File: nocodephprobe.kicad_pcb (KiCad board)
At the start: 2 copper layers, 76 x 80.9 mm, 34 parts, among them J1 RF1-01 BNC, J2 10K, Q1 2N7002, U1 LMV358a, U2 ICL7106CPL, U3 MCP1501T-10E/CHY, U4 VI-302-DP-RC-S, U5 L7805

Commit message: Remove fmask all the way around guard trace
Based on prototype pcbs from jlcpcb, I don't think solder bridges will
be an issue.
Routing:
- net BP: track 127.5 -> 125.7 mm, vias 3 -> 2
- net Net-(U2-INT): track 35.8 -> 35.0 mm
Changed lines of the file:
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@@
   (gr_line (start 122.297226 85.580302) (end 122.29625 85.580045)
     (stroke (width 0.132291) (type solid)) (layer "B.SilkS"))
+  (gr_line (start 156.9466 64.4906) (end 157.48 64.008)
+    (stroke (width 0.153) (type default)) (layer "F.Mask"))
   (gr_line (start 154.6098 64.389) (end 151.384 64.4144)
     (stroke (width 0.25) (type default)) (layer "F.Mask"))
+  (gr_line (start 159.766 63.754) (end 159.766 62.992)
+    (stroke (width 0.153) (type default)) (layer "F.Mask"))
+  (gr_line (start 149.606 67.818) (end 149.86 67.564)
+    (stroke (width 0.153) (type default)) (layer "F.Mask"))
+  (gr_line (start 159.766 62.992) (end 159.004 62.23)
+    (stroke (width 0.153) (type default)) (layer "F.Mask"))
+  (gr_line (start 157.48 64.008) (end 159.512 64.008)
+    (stroke (width 0.153) (type default)) (layer "F.Mask"))
+  (gr_line (start 149.86 67.564) (end 150.368 67.5132)
+    (stroke (width 0.153) (type default)) (layer "F.Mask"))
+  (gr_line (start 150.1648 65.532) (end 148.336 65.532)
+    (stroke (width 0.153) (type default)) (layer "F.Mask"))
+  (gr_line (start 148.082 67.818) (end 149.606 67.818)
+    (stroke (width 0.153) (type default)) (layer "F.Mask"))
   (gr_line (start 150.368 67.5132) (end 152.1714 65.786)
     (stroke (width 0.25) (type default)) (layer "F.Mask"))
@@
   (gr_line (start 158.2674 62.103) (end 157 62.103)
     (stroke (width 0.25) (type default)) (layer "F.Mask"))
+  (gr_line (start 148.336 65.532) (end 147.574 66.294)
+    (stroke (width 0.153) (type default)) (layer "F.Mask"))
+  (gr_line (start 159.512 64.008) (end 159.766 63.754)
+    (stroke (width 0.153) (type default)) (layer "F.Mask"))
   (gr_line (start 151.384 64.4144) (end 150.1648 65.532)
     (stroke (width 0.25) (type default)) (layer "F.Mask"))
@@
   (gr_line (start 155.7274 65.8114) (end 156.9466 64.4906)
     (stroke (width 0.25) (type default)) (layer "F.Mask"))
+  (gr_line (start 147.574 67.31) (end 148.082 67.818)
+    (stroke (width 0.153) (type default)) (layer "F.Mask"))
+  (gr_line (start 147.574 66.294) (end 147.574 67.31)
+    (stroke (width 0.153) (type default)) (layer "F.Mask"))
   (gr_line (start 110.7891 63.5254) (end 110.7891 69.249537)
     (stroke (width 0.127) (type solid)) (layer "Edge.Cuts"))
@@
   (segment (start 153.67 69.596) (end 154.813 68.453) (width 0.25) (layer "B.Cu") (net 10))
   (segment (start 154.813 68.453) (end 165.989 68.453) (width 0.25) (layer "B.Cu") (net 10))
-  (segment (start 158.486695 80.264) (end 159.647695 79.103) (width 0.25) (layer "F.Cu") (net 11))
-  (segment (start 157.009 79.802305) (end 157.470695 80.264) (width 0.25) (layer "F.Cu") (net 11))
-  (segment (start 163.957 77.530009) (end 164.652009 76.835) (width 0.25) (layer "F.Cu") (net 11))
-  (segment (start 166.497 84.583396) (end 173.062604 91.149) (width 0.25) (layer "F.Cu") (net 11))
-  (segment (start 157.470695 80.264) (end 158.486695 80.264) (width 0.25) (layer "F.Cu") (net 11))
-  (segment (start 165.608 76.835) (end 166.497 77.724) (width 0.25) (layer "F.Cu") (net 11))
-  (segment (start 173.062604 91.149) (end 177.329 91.149) (width 0.25) (layer "F.Cu") (net 11))
-  (segment (start 163.025991 79.103) (end 163.957 78.171991) (width 0.25) (layer "F.Cu") (net 11))
-  (segment (start 157.48 77.978) (end 157.009 78.449) (width 0.25) (layer "F.Cu") (net 11))
-  (segment (start 157.009 78.449) (end 157.009 79.802305) (width 0.25) (layer "F.Cu") (net 11))
-  (segment (start 177.329 91.149) (end 178.435 90.043) (width 0.25) (layer "F.Cu") (net 11))
-  (segment (start 163.957 78.171991) (end 163.957 77.530009) (width 0.25) (layer "F.Cu") (net 11))
-  (segment (start 164.652009 76.835) (end 165.608 76.835) (width 0.25) (layer "F.Cu") (net 11))
-  (segment (start 166.497 77.724) (end 166.497 84.583396) (width 0.25) (layer "F.Cu") (net 11))
-  (segment (start 159.647695 79.103) (end 163.025991 79.103) (width 0.25) (layer "F.Cu") (net 11))
+  (segment (start 163.685 77.7674) (end 163.685 78.443991) (width 0.25) (layer "F.Cu") (net 11))
+  (segment (start 164.5994 76.853) (end 163.685 77.7674) (width 0.25) (layer "F.Cu") (net 11))
+  (segment (start 178.435 87.493695) (end 173.020305 82.079) (width 0.25) (layer "F.Cu") (net 11))
+  (segment (start 157.433695 80.227) (end 156.680001 79.473306) (width 0.25) (layer "F.Cu") (net 11))
+  (segment (start 166.8664 82.132) (end 166.225 81.4906) (width 0.25) (layer "F.Cu") (net 11))
+  (segment (start 159.114905 79.1464) (end 158.034305 80.227) (width 0.25) (layer "F.Cu") (net 11))
+  (segment (start 156.680001 78.777999) (end 157.48 77.978) (width 0.25) (layer "F.Cu") (net 11))
+  (segment (start 163.685 78.443991) (end 162.982591 79.1464) (width 0.25) (layer "F.Cu") (net 11))
+  (segment (start 156.680001 79.473306) (end 156.680001 78.777999) (width 0.25) (layer "F.Cu") (net 11))
+  (segment (start 167.6284 82.079) (end 167.5754 82.132) (width 0.25) (layer "F.Cu") (net 11))
+  (segment (start 173.020305 82.079) (end 167.6284 82.079) (width 0.25) (layer "F.Cu") (net 11))
+  (segment (start 162.982591 79.1464) (end 159.114905 79.1464) (width 0.25) (layer "F.Cu") (net 11))
+  (segment (start 167.5754 82.132) (end 166.8664 82.132) (width 0.25) (layer "F.Cu") (net 11))
+  (segment (start 178.435 90.043) (end 178.435 87.493695) (width 0.25) (layer "F.Cu") (net 11))
+  (segment (start 166.225 81.4906) (end 166.225 77.512009) (width 0.25) (layer "F.Cu") (net 11))
+  (segment (start 158.034305 80.227) (end 157.433695 80.227) (width 0.25) (layer "F.Cu") (net 11))
+  (segment (start 166.225 77.512009) (end 165.565991 76.853) (width 0.25) (layer "F.Cu") (net 11))
+  (segment (start 165.565991 76.853) (end 164.5994 76.853) (width 0.25) (layer "F.Cu") (net 11))
   (segment (start 178.689 117.586) (end 177.487 116.384) (width 0.25) (layer "F.Cu") (net 12))
   (segment (start 162.477 109.077) (end 161.9 108.5) (width 0.25) (layer "F.Cu") (net 12))
@@
   (segment (start 165.281 109.077) (end 162.477 109.077) (width 0.25) (layer "F.Cu") (net 12))
   (segment (start 143.315 101.435) (end 142.367 102.383) (width 0.25) (layer "F.Cu") (net 13))
+  (segment (start 172.72 100.858) (end 173.845 99.733) (width 0.25) (layer "F.Cu") (net 13))
   (segment (start 154.94 100.858) (end 153.865 101.933) (width 0.25) (layer "F.Cu") (net 13))
+  (segment (start 173.845 99.733) (end 173.845 83.929) (width 0.25) (layer "F.Cu") (net 13))
   (segment (start 145.855 100.41272) (end 145.22528 99.783) (width 0.25) (layer "F.Cu") (net 13))
-  (segment (start 172.72 82.804) (end 172.72 88.519) (width 0.25) (layer "F.Cu") (net 13))
   (segment (start 130.863297 71.681297) (end 142.504659 71.681297) (width 0.25) (layer "F.Cu") (net 13))
   (segment (start 172.72 100.858) (end 171.645 101.933) (width 0.25) (layer "F.Cu") (net 13))
@@
   (segment (start 129.54 70.358) (end 130.863297 71.681297) (width 0.25) (layer "F.Cu") (net 13))
   (segment (start 136.145 102.383) (end 134.62 100.858) (width 0.25) (layer "F.Cu") (net 13))
+  (segment (start 173.845 83.929) (end 172.72 82.804) (width 0.25) (layer "F.Cu") (net 13))
   (segment (start 127 70.358) (end 129.54 70.358) (width 0.25) (layer "F.Cu") (net 13))
   (segment (start 124.46 70.358) (end 127 70.358) (width 0.25) (layer "F.Cu") (net 13))
@@
   (segment (start 144.282 99.783) (end 143.315 100.75) (width 0.25) (layer "F.Cu") (net 13))
   (segment (start 171.645 101.933) (end 156.015 101.933) (width 0.25) (layer "F.Cu") (net 13))
-  (segment (start 172.72 88.519) (end 174.625 90.424) (width 0.25) (layer "F.Cu") (net 13))
   (segment (start 145.22528 99.783) (end 144.282 99.783) (width 0.25) (layer "F.Cu") (net 13))
   (via (at 172.72 82.804) (size 0.8) (drill 0.4) (layers "F.Cu" "B.Cu") (net 13))
   (via (at 142.504659 71.681297) (size 0.8) (drill 0.4) (layers "F.Cu" "B.Cu") (net 13))
-  (via (at 174.625 90.424) (size 0.8) (drill 0.4) (layers "F.Cu" "B.Cu") (net 13))
-  (segment (start 162.433 71.755) (end 163.83 71.755) (width 0.25) (layer "B.Cu") (net 13))
-  (segment (start 174.625 90.424) (end 174.625 94.644197) (width 0.25) (layer "B.Cu") (net 13))
-  (segment (start 163.83 71.755) (end 168.783 76.708) (width 0.25) (layer "B.Cu") (net 13))
-  (segment (start 168.783 76.708) (end 171.45 76.708) (width 0.25) (layer "B.Cu") (net 13))
-  (segment (start 161.163 69.977) (end 161.163 70.485) (width 0.25) (layer "B.Cu") (net 13))
-  (segment (start 174.625 94.644197) (end 172.72 96.549197) (width 0.25) (layer "B.Cu") (net 13))
-  (segment (start 161.163 70.485) (end 162.433 71.755) (width 0.25) (layer "B.Cu") (net 13))
-  (segment (start 156.015 69.283) (end 160.469 69.283) (width 0.25) (layer "B.Cu") (net 13))
+  (segment (start 172.72 77.978) (end 166.5932 71.8512) (width 0.25) (layer "B.Cu") (net 13))
+  (segment (start 156.4332 71.8512) (end 154.94 70.358) (width 0.25) (layer "B.Cu") (net 13))
+  (segment (start 166.5932 71.8512) (end 156.4332 71.8512) (width 0.25) (layer "B.Cu") (net 13))
   (segment (start 153.616703 71.681297) (end 154.94 70.358) (width 0.25) (layer "B.Cu") (net 13))
-  (segment (start 154.94 70.358) (end 156.015 69.283) (width 0.25) (layer "B.Cu") (net 13))
-  (segment (start 160.469 69.283) (end 161.163 69.977) (width 0.25) (layer "B.Cu") (net 13))
-  (segment (start 171.45 76.708) (end 172.72 77.978) (width 0.25) (layer "B.Cu") (net 13))
   (segment (start 142.504659 71.681297) (end 153.616703 71.681297) (width 0.25) (layer "B.Cu") (net 13))
-  (segment (start 172.72 96.549197) (end 172.72 100.858) (width 0.25) (layer "B.Cu") (net 13))
   (segment (start 172.72 82.804) (end 172.72 77.978) (width 0.25) (layer "B.Cu") (net 13))
   (segment (start 158.2166 58.2516) (end 158.2166 60.6022) (width 0.25) (layer "F.Cu") (net 14))

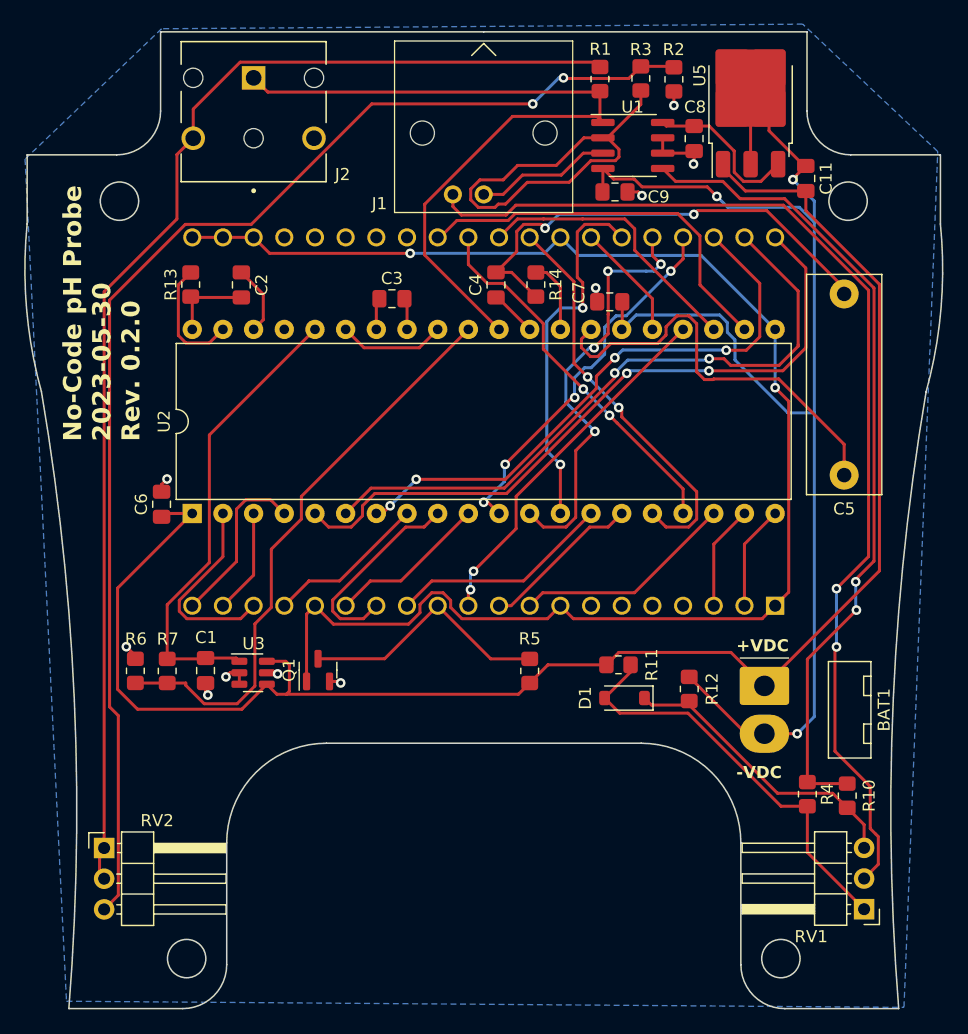
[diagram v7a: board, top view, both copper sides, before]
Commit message: pcb: fix lcd footprint
The pins are actually 1.27mm offset (so a 2.54mm wider footprint):

https://media.digikey.com/pdf/Data%20Sheets/Varitronix%20PDFs/Displays.pdf
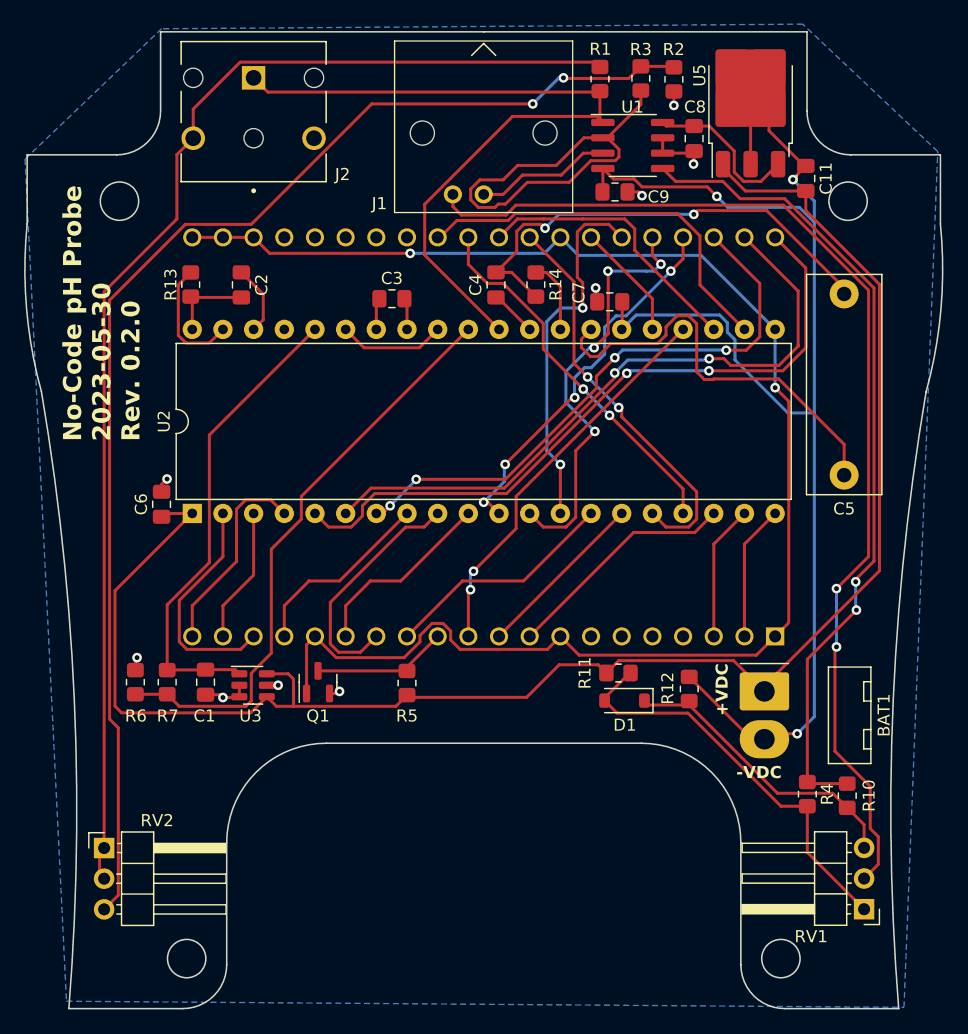
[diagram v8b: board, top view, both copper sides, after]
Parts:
- moved R5 10.2 mm to (142.2, 107.3)
- moved U4 1.27 mm to (172.7, 102.1)
- moved U3 1.03 mm to (129.5, 107.4)
- moved Q1 1.00 mm to (134.9, 107.2)
- moved C1 0.96 mm to (125.6, 107.2)
- moved R6 0.94 mm to (119.8, 107.2)
- moved R7 0.93 mm to (122.4, 107.2)
- moved R11 0.68 mm to (159.8, 106.4)
- moved BAT1 0.46 mm to (171.8, 108.0)
- moved D1 0.21 mm to (160.2, 108.7)
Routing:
- net DP: track 21.2 -> 11.1 mm
- net Net-(U2-D2): track 16.9 -> 20.0 mm
- net Net-(U2-C3): track 30.2 -> 32.8 mm
- net Net-(U2-POL): track 8.69 -> 11.2 mm
- net Net-(U2-E1): track 13.3 -> 15.9 mm
- net Net-(U2-D1): track 16.4 -> 19.0 mm
- net Net-(U2-C2): track 13.3 -> 15.9 mm
- net Net-(U2-C1): track 8.69 -> 11.2 mm
- net Net-(U2-B1): track 14.3 -> 16.8 mm
- net Net-(U2-AB4): track 8.69 -> 11.2 mm
- net +VDC: track 137.6 -> 139.9 mm
- net BP: track 125.7 -> 127.2 mm
- net Net-(U2-D3): track 13.3 -> 14.4 mm
- net Net-(U2-E3): track 18.4 -> 19.5 mm
- net Net-(U2-E2): track 18.4 -> 19.5 mm
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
